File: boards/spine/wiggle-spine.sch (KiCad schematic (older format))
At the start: 1 part

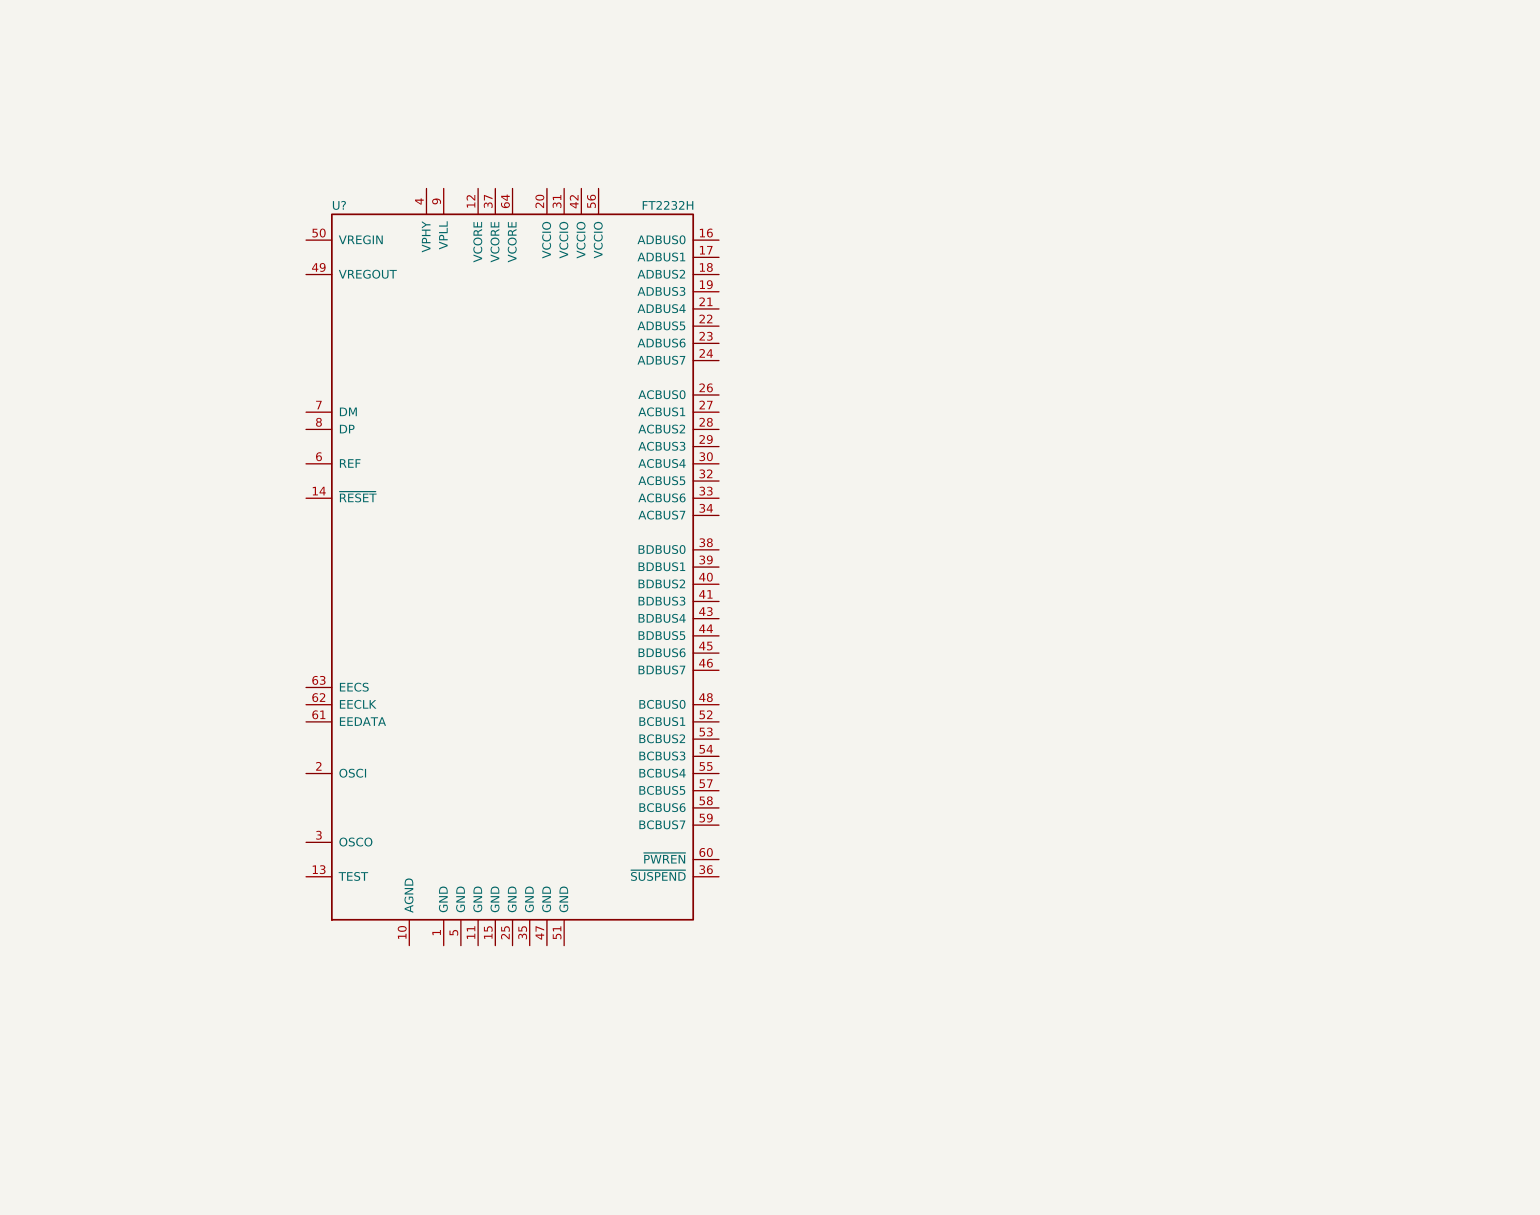
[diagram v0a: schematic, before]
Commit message: Untested draft of the DMX isolator subcircuit
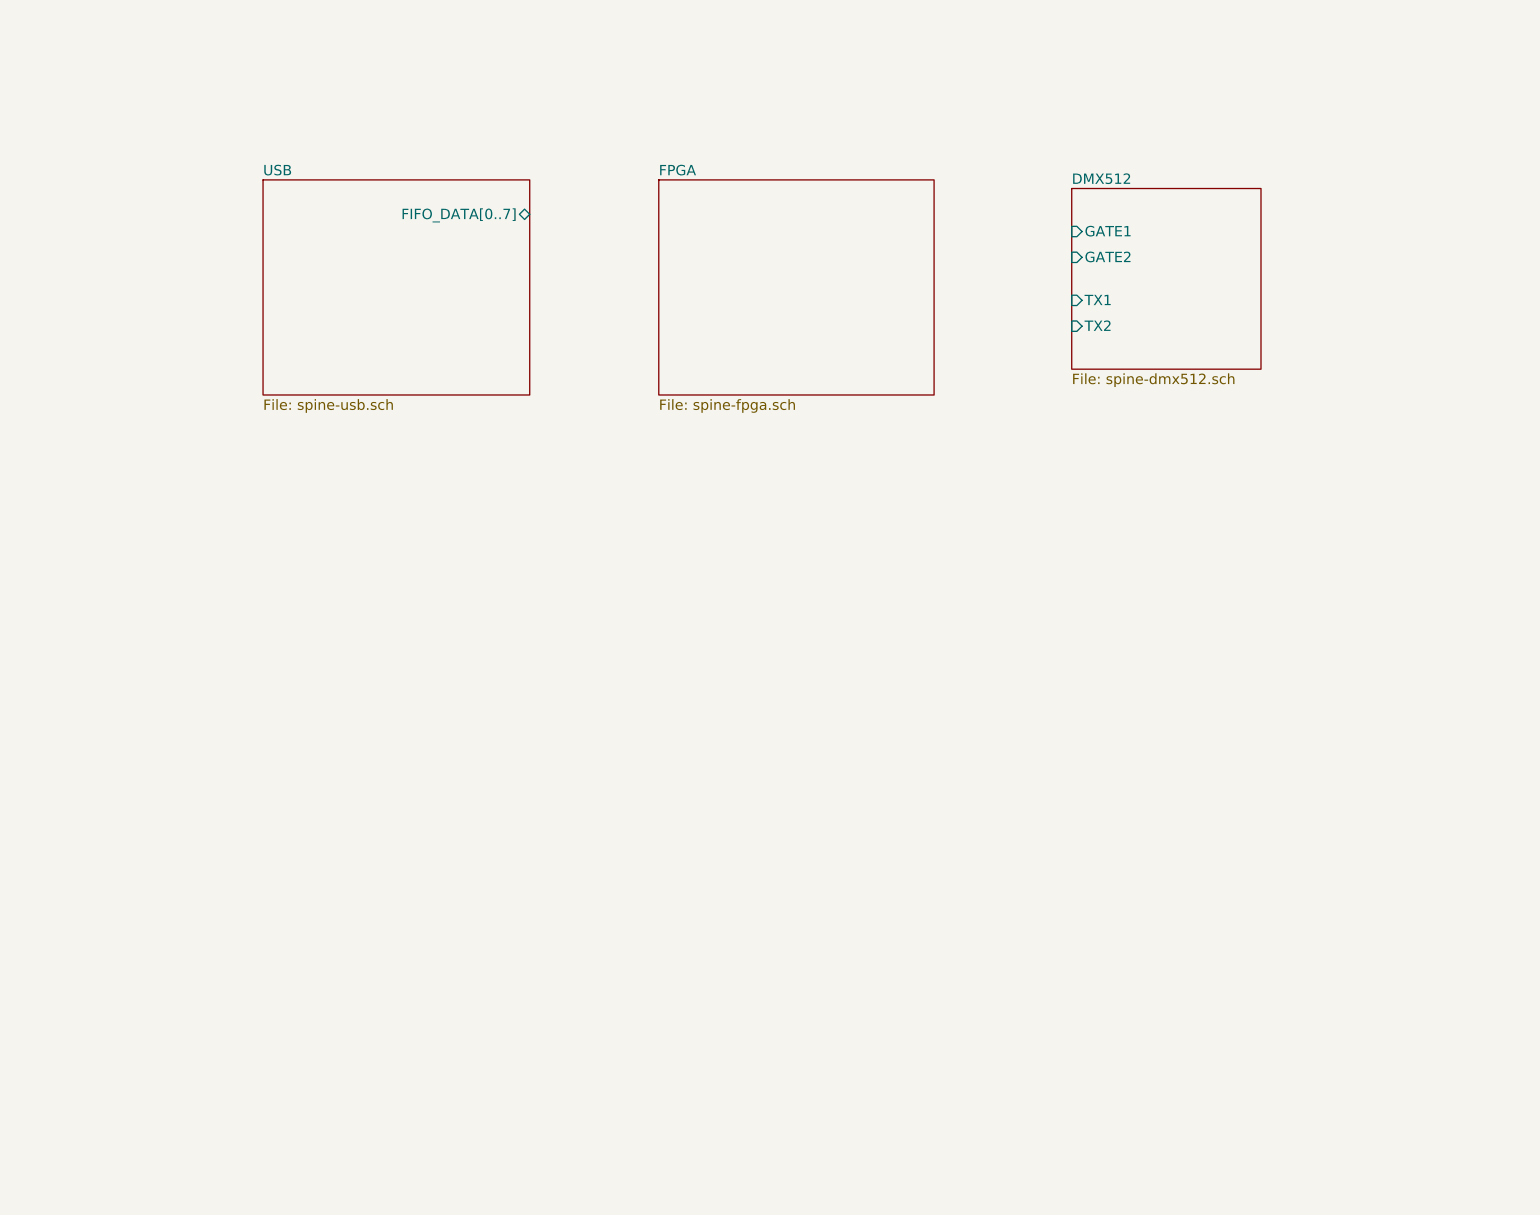
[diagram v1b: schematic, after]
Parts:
- removed U?: FT2232H, symbol FT2232H
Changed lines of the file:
@@
 LIBS:ftdi
 LIBS:Lattice
+LIBS:silabs
+LIBS:Cypress_cy8c5xlp
+LIBS:Cypress_PSoC
+LIBS:Lattice_iCE_FPGA
+LIBS:xess
+LIBS:xilinx6s
+LIBS:xilinx6v
+LIBS:xilinx7
+LIBS:wiggle-spine-cache
 EELAYER 25 0
 EELAYER END
-$Descr A4 11693 8268
+$Descr USLetter 11000 8500
 encoding utf-8
-Sheet 1 1
+Sheet 1 4
 Title ""
 Date ""
@@
 Comment4 ""
 $EndDescr
-$Comp
-L FT2232H U?
-U 1 1 562EE927
-P 4150 4250
-F 0 "U?" H 3100 6350 50  0000 L CNN
-F 1 "FT2232H" H 4900 6350 50  0000 L CNN
-F 2 "" H 4150 4250 50  0000 C CNN
-F 3 "" H 4150 4250 50  0000 C CNN
-	1    4150 4250
-	1    0    0    -1
-$EndComp
+$Sheet
+S 2700 2000 1550 1250
+U 5637B4E6
+F0 "USB" 60
+F1 "spine-usb.sch" 60
+F2 "FIFO_DATA[0..7]" B R 4250 2200 60
+$EndSheet
+$Sheet
+S 5000 2000 1600 1250
+U 5637E2EA
+F0 "FPGA" 60
+F1 "spine-fpga.sch" 60
+$EndSheet
+$Sheet
+S 7400 2050 1100 1050
+U 563E737A
+F0 "DMX512" 60
+F1 "spine-dmx512.sch" 60
+F2 "GATE1" I L 7400 2300 60
+F3 "GATE2" I L 7400 2450 60
+F4 "TX1" I L 7400 2700 60
+F5 "TX2" I L 7400 2850 60
+$EndSheet
 $EndSCHEMATC

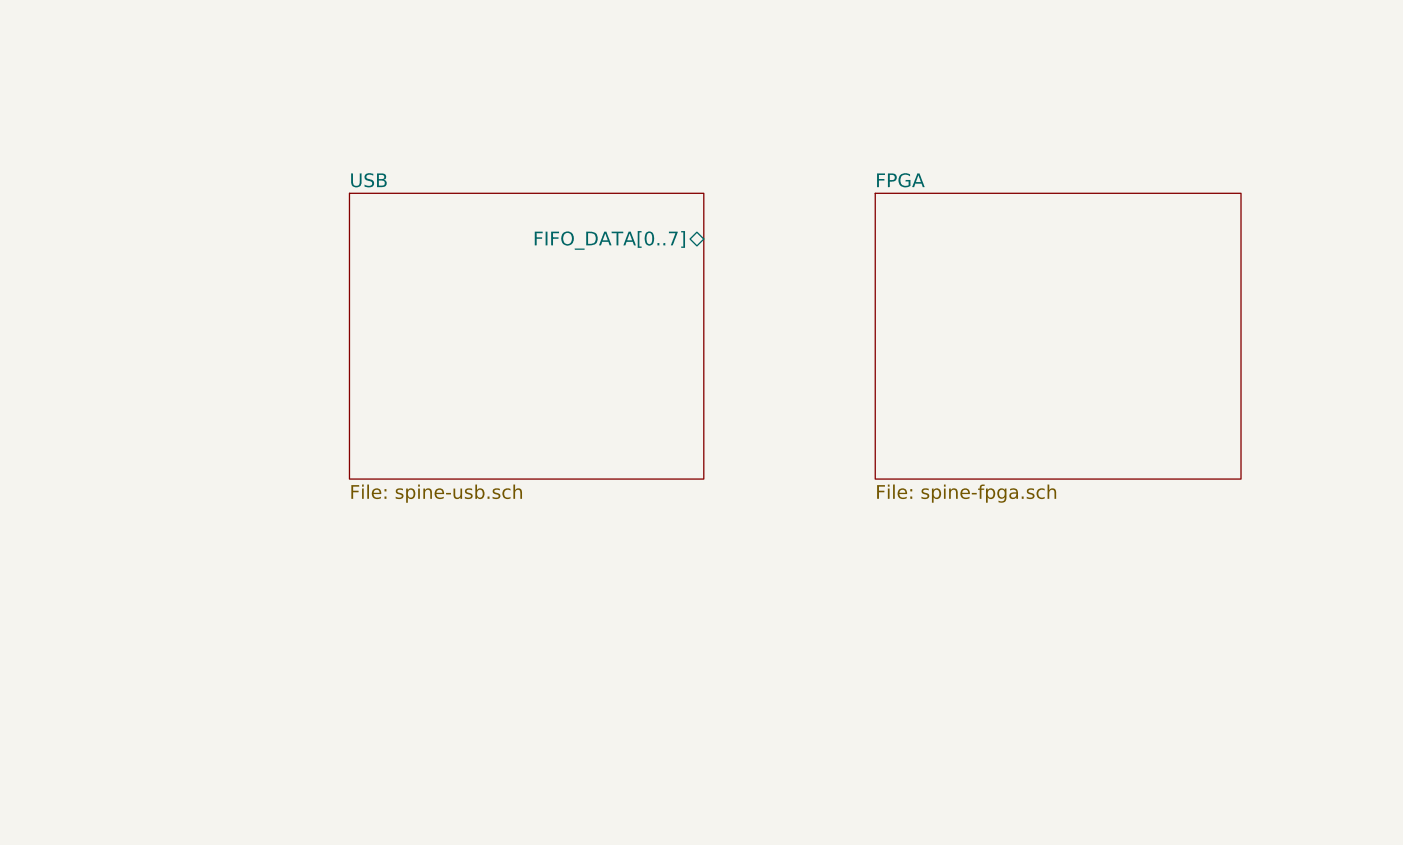
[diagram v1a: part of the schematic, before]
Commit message: More schematic work: module ports and USB
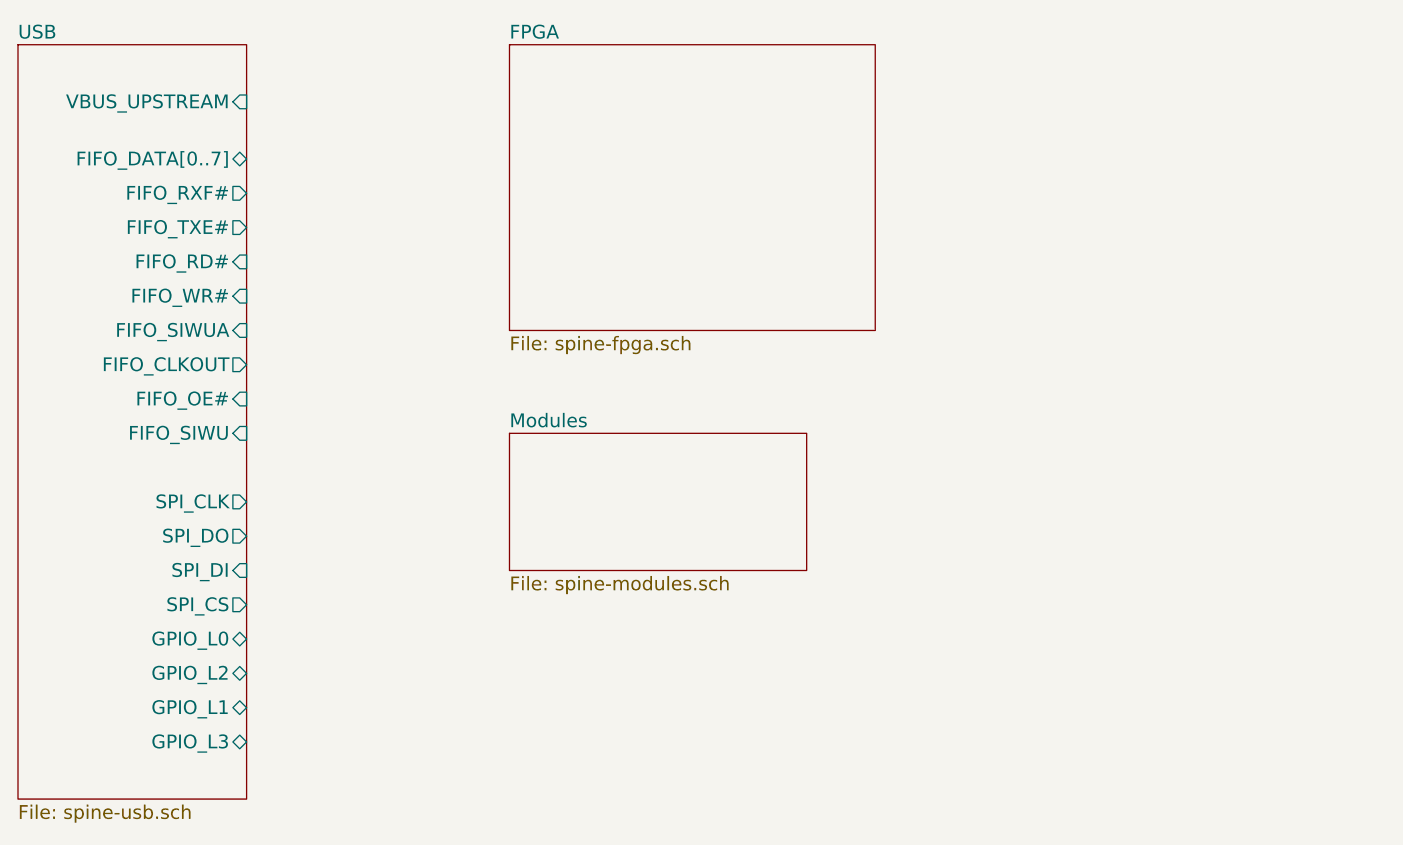
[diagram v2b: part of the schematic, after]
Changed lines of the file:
@@
 $Descr USLetter 11000 8500
 encoding utf-8
-Sheet 1 4
+Sheet 1 5
 Title ""
 Date ""
@@
 $EndDescr
 $Sheet
-S 2700 2000 1550 1250
+S 1250 1350 1000 3300
 U 5637B4E6
 F0 "USB" 60
 F1 "spine-usb.sch" 60
-F2 "FIFO_DATA[0..7]" B R 4250 2200 60
+F2 "FIFO_DATA[0..7]" B R 2250 1850 60
+F3 "VBUS_UPSTREAM" I R 2250 1600 60
+F4 "FIFO_RXF#" O R 2250 2000 60
+F5 "FIFO_TXE#" O R 2250 2150 60
+F6 "FIFO_RD#" I R 2250 2300 60
+F7 "FIFO_WR#" I R 2250 2450 60
+F8 "FIFO_SIWUA" I R 2250 2600 60
+F9 "FIFO_CLKOUT" O R 2250 2750 60
+F10 "FIFO_OE#" I R 2250 2900 60
+F11 "FIFO_SIWU" I R 2250 3050 60
+F12 "SPI_CLK" O R 2250 3350 60
+F13 "SPI_DO" O R 2250 3500 60
+F14 "SPI_DI" I R 2250 3650 60
+F15 "SPI_CS" O R 2250 3800 60
+F16 "GPIO_L0" B R 2250 3950 60
+F17 "GPIO_L2" B R 2250 4100 60
+F18 "GPIO_L1" B R 2250 4250 60
+F19 "GPIO_L3" B R 2250 4400 60
 $EndSheet
 $Sheet
-S 5000 2000 1600 1250
+S 3400 1350 1600 1250
 U 5637E2EA
 F0 "FPGA" 60
@@
 F5 "TX2" I L 7400 2850 60
 $EndSheet
+$Sheet
+S 3400 3050 1300 600
+U 5641D2D7
+F0 "Modules" 60
+F1 "spine-modules.sch" 60
+$EndSheet
 $EndSCHEMATC
